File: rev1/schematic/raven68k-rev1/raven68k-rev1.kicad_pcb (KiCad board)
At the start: 4 copper layers, 208.3 x 114.3 mm, 82 parts, among them IC1 L5970D013TR, IC2 L5970D013TR, J1 CPLD_JTAG, J2 DUART_IO, J3 RAPC722BK, SW1 RESET_SW, U1 MCP100-465D, U10 28C256, U11 28C256, U2 68010D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

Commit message: additional mounting standoff near pressure area
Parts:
- added REF**: MountingHole_4mm, MountingHole:MountingHole_4mm, F.Cu at (212.9, 56.1)
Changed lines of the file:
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@@
     )
   )
+  (footprint "MountingHole:MountingHole_4mm" (layer "F.Cu")
+    (at 212.852 56.134)
+    (descr "Mounting Hole 4mm, no annular")
+    (tags "mounting hole 4mm no annular")
+    (attr exclude_from_pos_files exclude_from_bom)
+    (fp_text reference "REF**" (at 0 -5) (layer "F.SilkS")
+      (effects (font (size 1 1) (thickness 0.15)))
+    )
+    (fp_text value "MountingHole_4mm" (at 0 5) (layer "F.Fab")
+      (effects (font (size 1 1) (thickness 0.15)))
+    )
+    (fp_text user "${REFERENCE}" (at 0.3 0) (layer "F.Fab")
+      (effects (font (size 1 1) (thickness 0.15)))
+    )
+    (fp_circle (center 0 0) (end 4 0) (layer "Cmts.User") (width 0.15) (fill none))
+    (fp_circle (center 0 0) (end 4.25 0) (layer "F.CrtYd") (width 0.05) (fill none))
+    (pad "" np_thru_hole circle (at 0 0) (size 4 4) (drill 4) (layers *.Cu *.Mask))
+  )
   (footprint "Diode_SMD:D_1206_3216Metric_Pad1.42x1.75mm_HandSolder" (layer "F.Cu")
     (at 195.58 49.53)
@@
     (connect_pads (clearance 0.508))
     (min_thickness 0.254) (filled_areas_thickness no)
-    (fill (thermal_gap 0.508) (thermal_bridge_width 0.508))
+    (fill yes (thermal_gap 0.508) (thermal_bridge_width 0.508))
     (polygon
       (pts

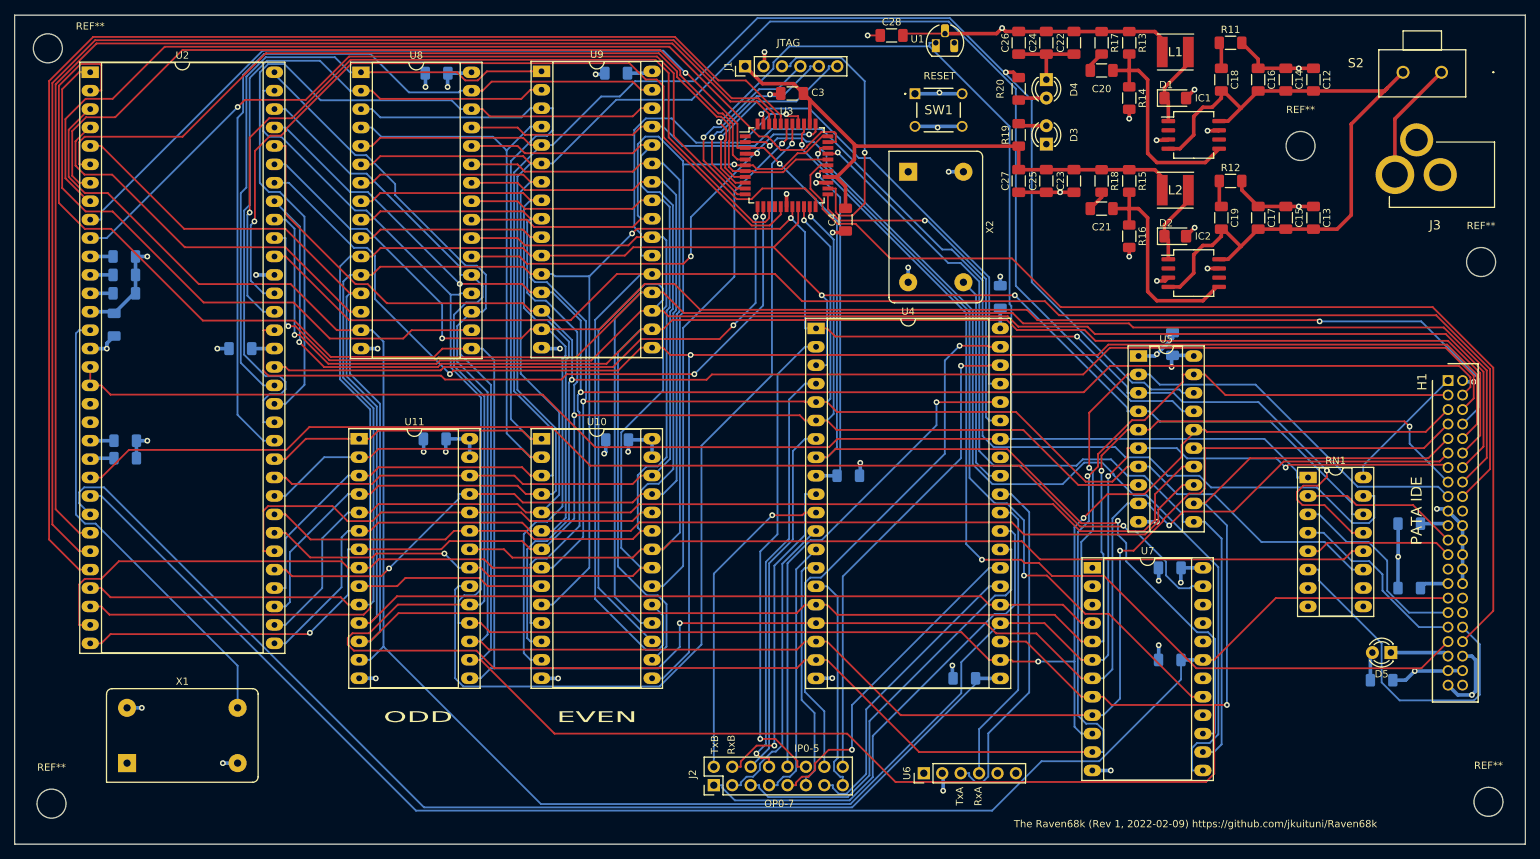
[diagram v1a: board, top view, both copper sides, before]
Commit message: bad footprint on rev1
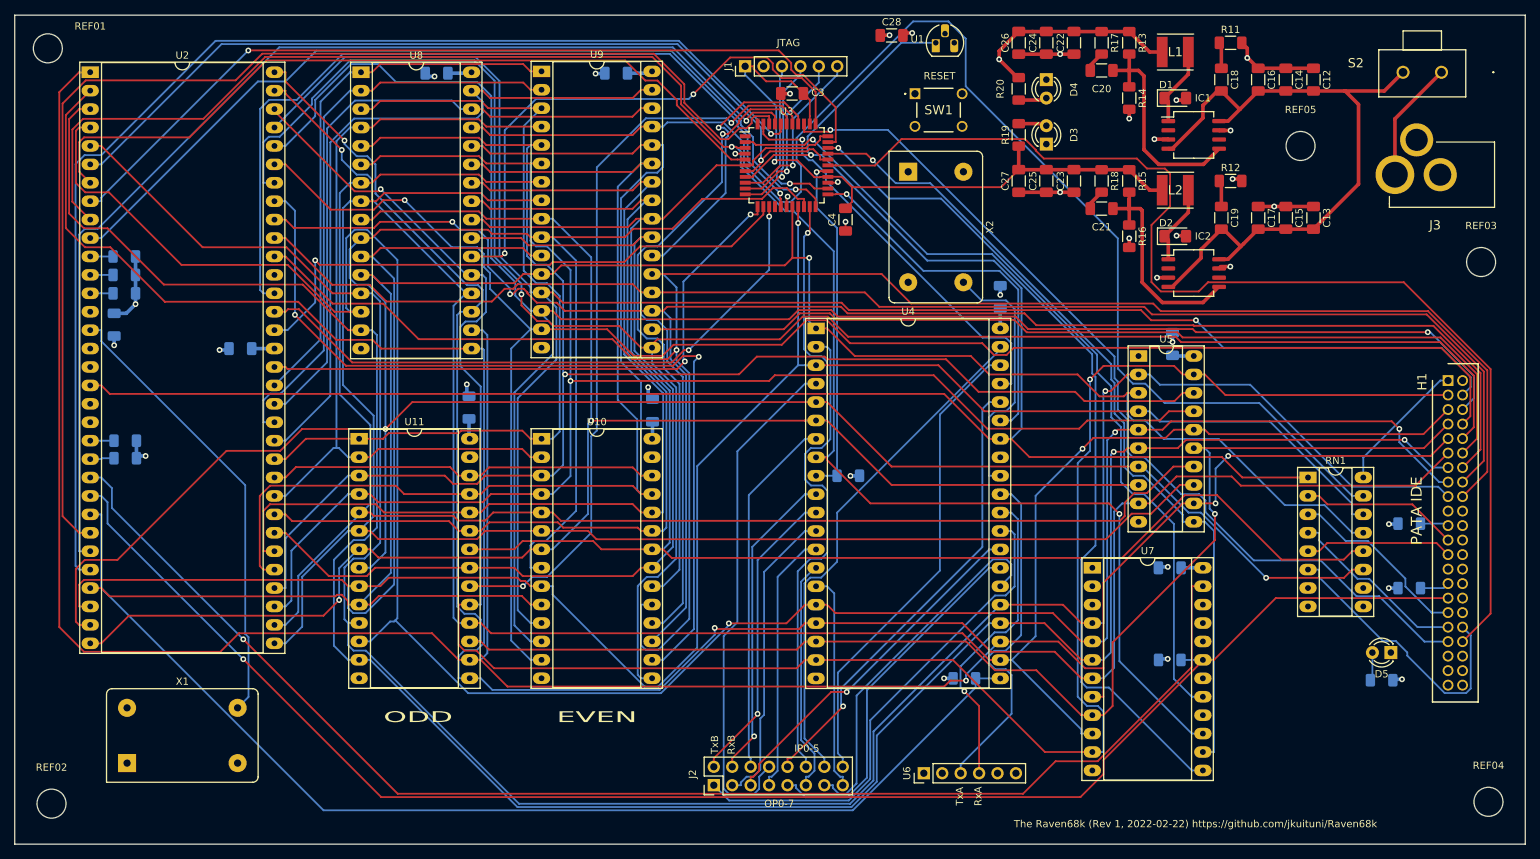
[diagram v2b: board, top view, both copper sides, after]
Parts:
- C26, C27: value 100nF -> 0.1uF
- moved C10 6.40 mm to (98.2, 92.2), turned to 90 degrees
- moved C11 6.34 mm to (123.5, 92.6), turned to 90 degrees
- renumbered REF** to REF01, REF** to REF02, REF** to REF03, REF** to REF04, REF** to REF05
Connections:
- net NOT_DS renamed NOT_LDS
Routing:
- net GND: track 148.3 -> 69.5 mm, vias 42 -> 28
- net A3: track 303.0 -> 378.4 mm
- net +5V: track 132.9 -> 76.5 mm, vias 17 -> 10
- net A2: track 293.8 -> 340.5 mm, vias 2 -> 1
- net A7: track 262.0 -> 217.1 mm, vias 0 -> 1
- net A8: track 258.2 -> 217.4 mm, vias 0 -> 1
- net D11: track 241.8 -> 278.2 mm, vias 2 -> 1
- net A22: track 118.9 -> 85.4 mm, vias 1 -> 2
- net D1: track 291.8 -> 322.9 mm, vias 2 -> 3
- net A1: track 317.5 -> 287.7 mm, vias 4 -> 1
- net D8: track 228.1 -> 255.6 mm, vias 2 -> 1
- net D0: track 290.7 -> 317.8 mm
- net ~{ROM_LCE}: track 128.2 -> 103.2 mm, vias 1 -> 2
- net ~{IPL2}: track 166.8 -> 191.4 mm
- net D9: track 237.5 -> 260.8 mm
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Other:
- board text added: "The Raven68k (Rev 1, 2022-02-22) https://github.com/jkuituni/Raven68k"
- board text removed: "The Raven68k (Rev 1, 2022-02-09) https://github.com/jkuituni/Raven68k"
